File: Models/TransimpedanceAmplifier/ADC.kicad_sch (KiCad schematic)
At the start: 8 parts, among them U3 ADS8699IPW

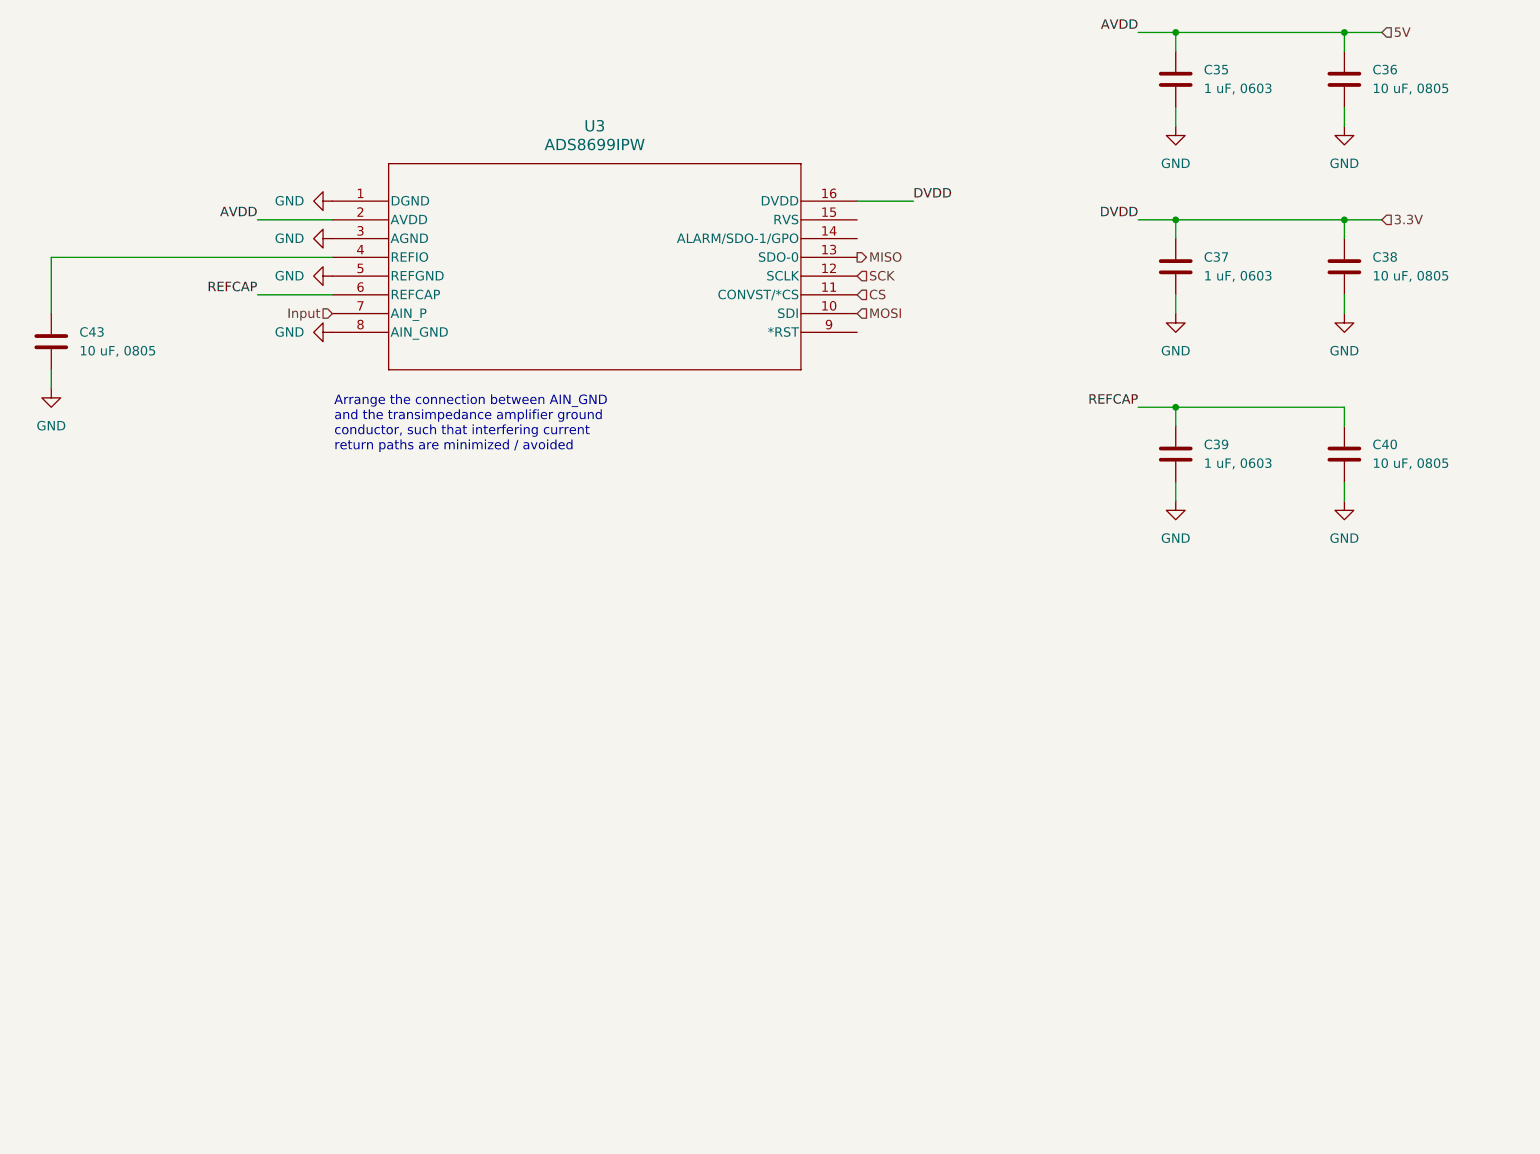
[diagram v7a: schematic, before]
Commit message: Connected all pins of the data converters
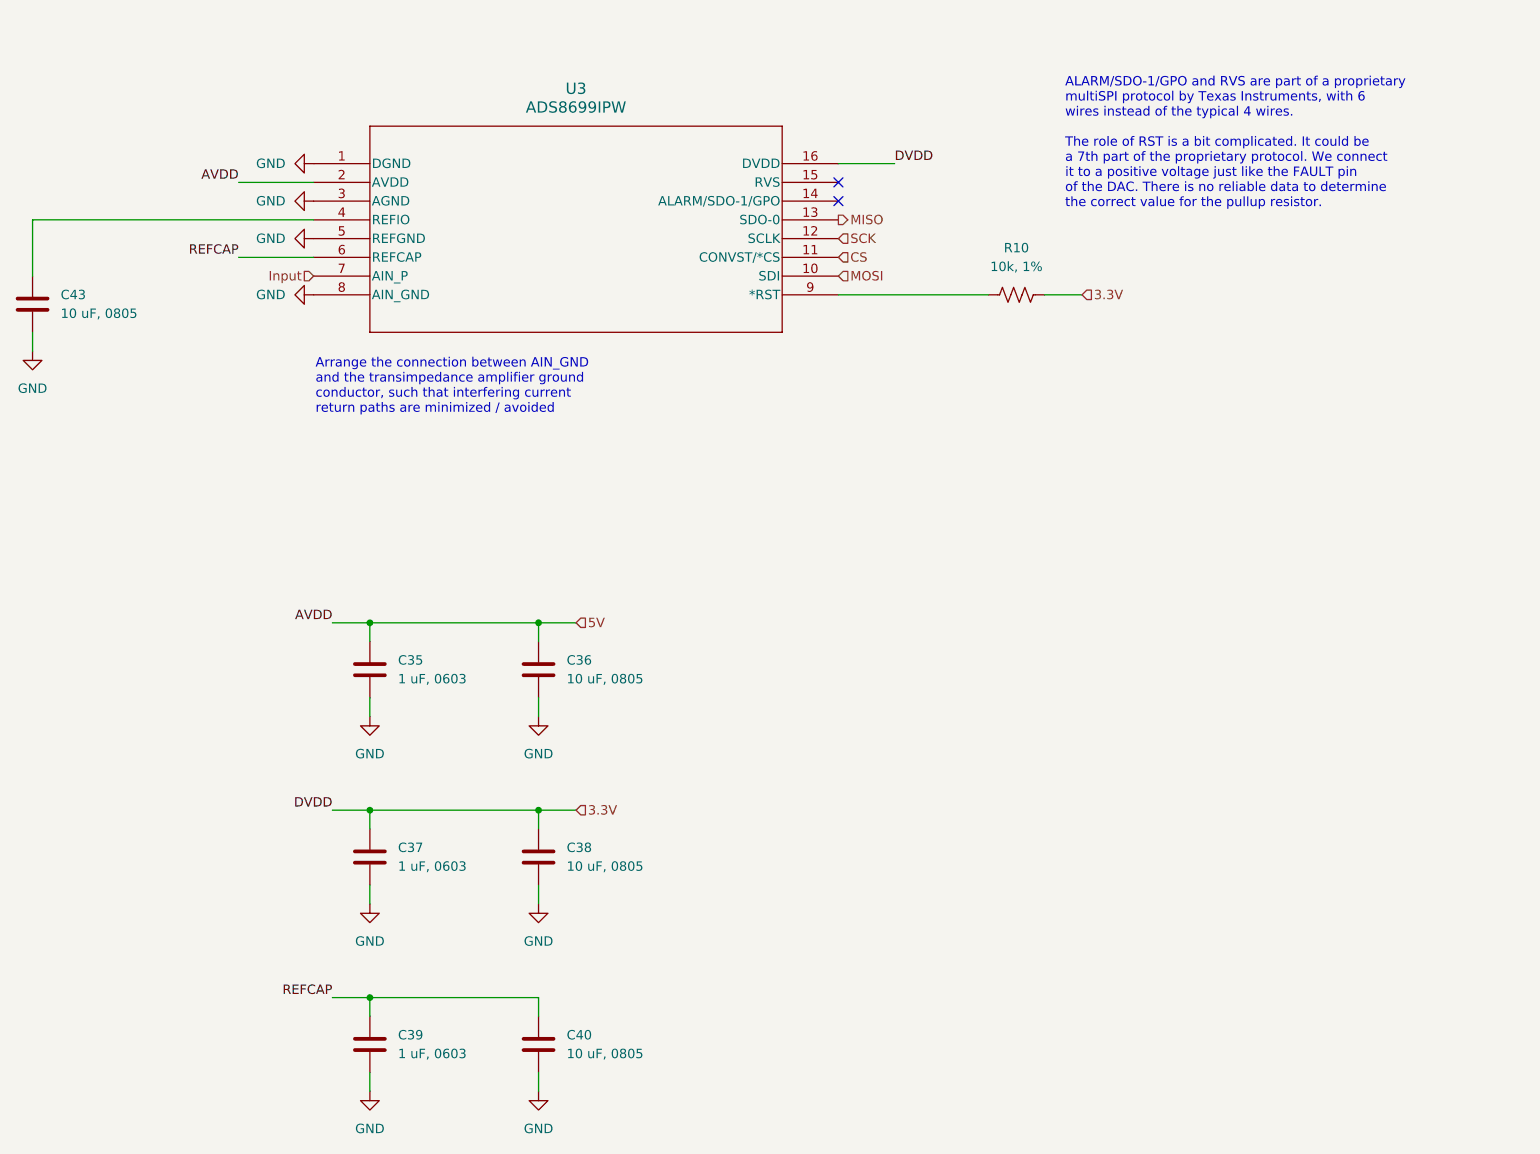
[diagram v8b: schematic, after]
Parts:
- added R10: 10k, 1%, symbol Device:R_US
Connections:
- net 3.3V: now also R10.2
- net at U3.9 (*RST): now also R10.1
- no-connect marks 0 -> 2
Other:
- note added: "ALARM/SDO-1/GPO and RVS are part of a proprietary multiSPI protocol by Texas Instruments, with 6 wires instead of the typical 4 wires. The role of RST is a bit complicated. It could be a 7th part of the proprietary protocol. We connect it to a positive voltage just like the FAULT pin of the DAC. There is no reliable data to determine the correct value for the pullup resistor."
- moved on the sheet: C35, C36, C37, C38, C39, C40, C43, U3
